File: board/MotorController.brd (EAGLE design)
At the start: 41.6 x 33 mm, 9 parts, among them IC1 7805TV, U1 ATTINY85-20P

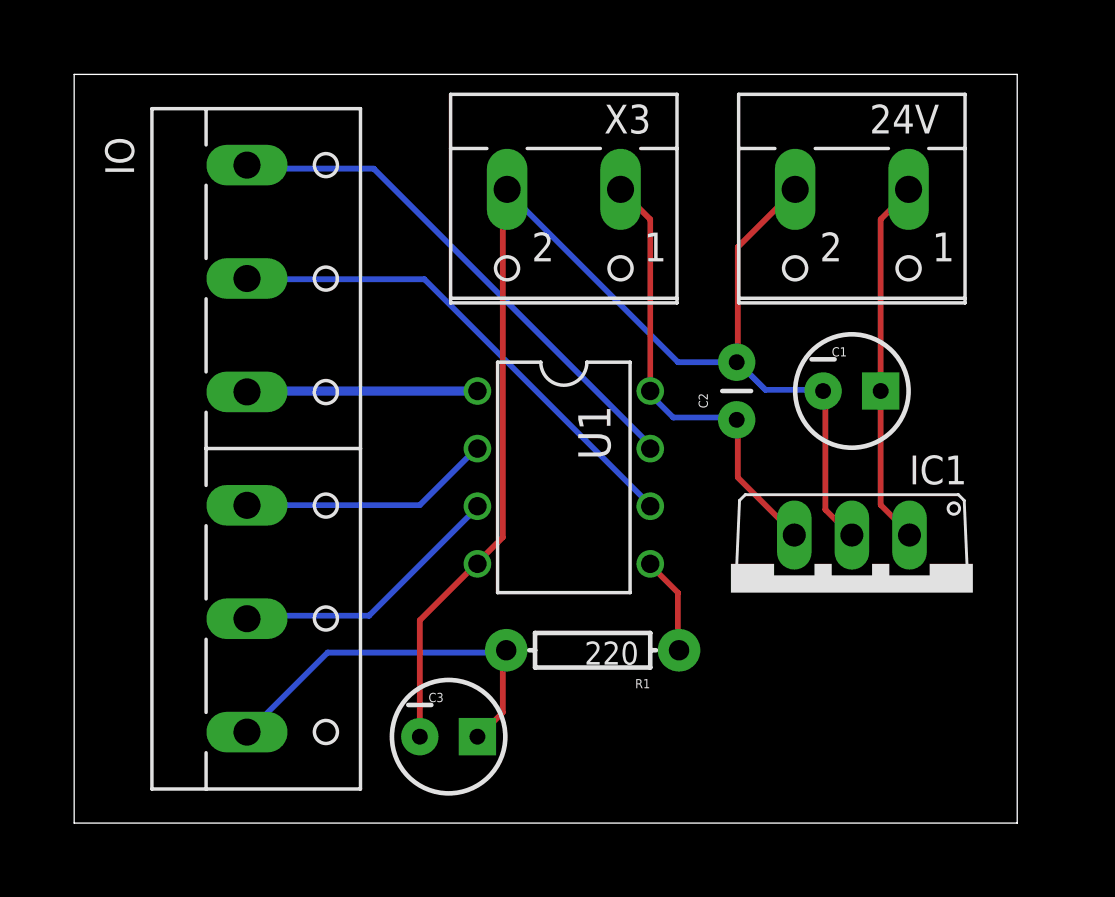
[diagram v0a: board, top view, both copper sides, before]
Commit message: Add a ground pour on the bottom plane and route all power and signal traces on the top
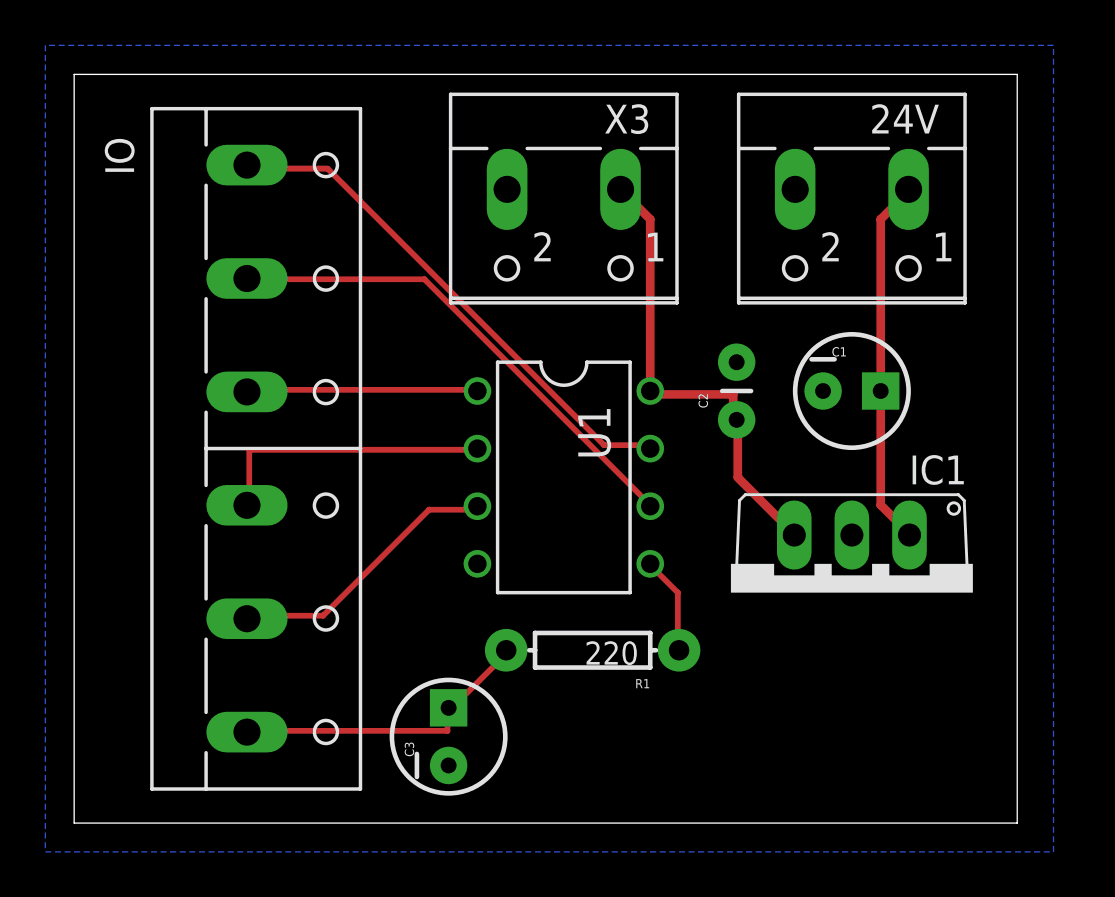
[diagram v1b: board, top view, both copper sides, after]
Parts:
- turned C3 to 90 degrees
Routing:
- net GND: track 59.1 -> 0.00 mm
- net VSPD: track 17.3 -> 13.6 mm
- net N$3: track 11.2 -> 12.6 mm
- net VCC: track 20.0 -> 20.6 mm
- added copper zone on layer 16, net GND

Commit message: Tweaked schematic
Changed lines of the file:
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@@
 <signal name="GND">
 <contactref element="C3" pad="2"/>
-<contactref element="X3" pad="2"/>
 <contactref element="IC1" pad="2"/>
 <contactref element="24V" pad="2"/>
@@
 <vertex x="-1.27" y="34.29"/>
 </polygon>
+<contactref element="X3" pad="2"/>
 </signal>
 <signal name="N$6">
@@
 <contactref element="U1" pad="8"/>
 <contactref element="IC1" pad="3"/>
-<contactref element="X3" pad="1"/>
 <contactref element="C2" pad="1"/>
 <wire x1="29.0576" y1="18.8976" x2="25.4" y2="18.8976" width="0.381" layer="1"/>
@@
 <wire x1="25.4" y1="26.6192" x2="24.1808" y2="27.8384" width="0.381" layer="1"/>
 <wire x1="25.4" y1="19.05" x2="25.4" y2="26.6192" width="0.381" layer="1"/>
-<wire x1="24.1808" y1="27.8384" x2="24.09" y2="27.94" width="0.381" layer="1"/>
+<contactref element="X3" pad="1"/>
+<wire x1="24.1808" y1="27.8384" x2="24.09" y2="27.94" width="0" layer="19" extent="1-1"/>
 </signal>
 <signal name="+24V" class="1">

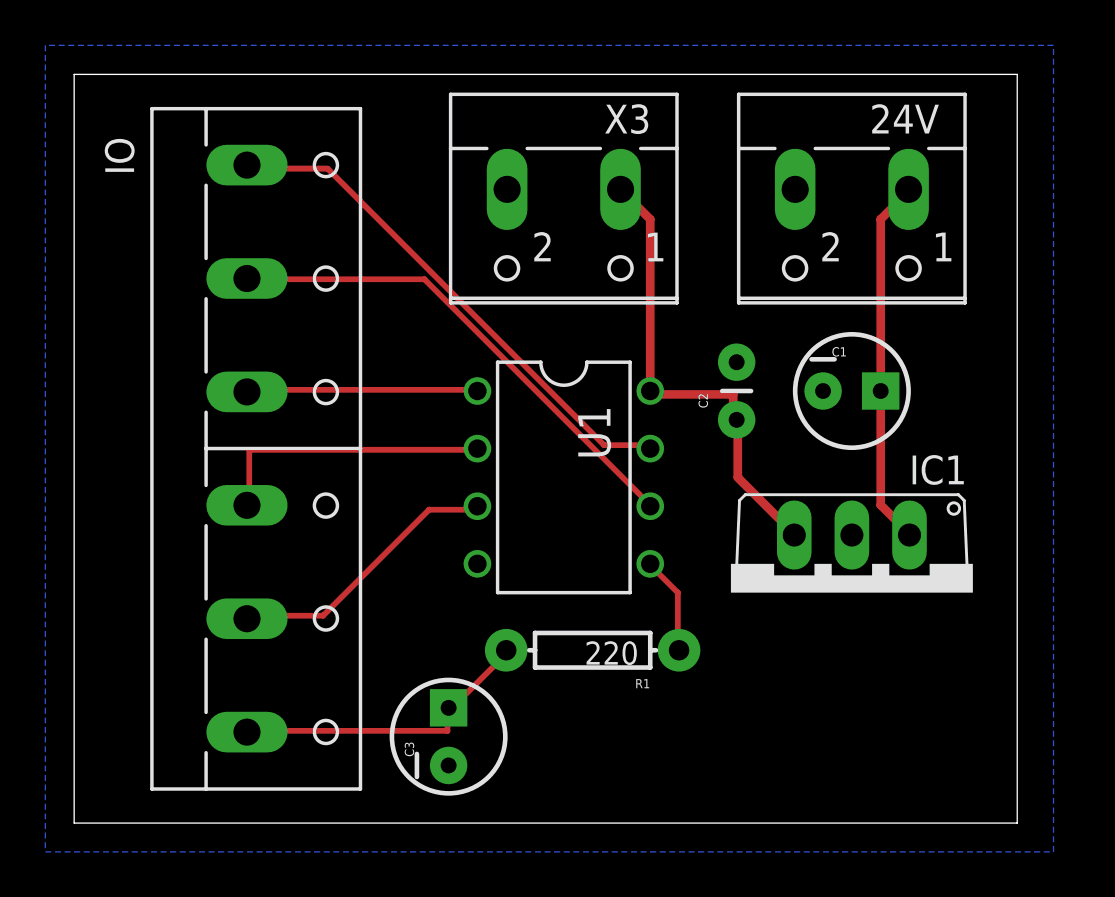
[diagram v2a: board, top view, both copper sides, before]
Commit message: Switch to a top GND pour
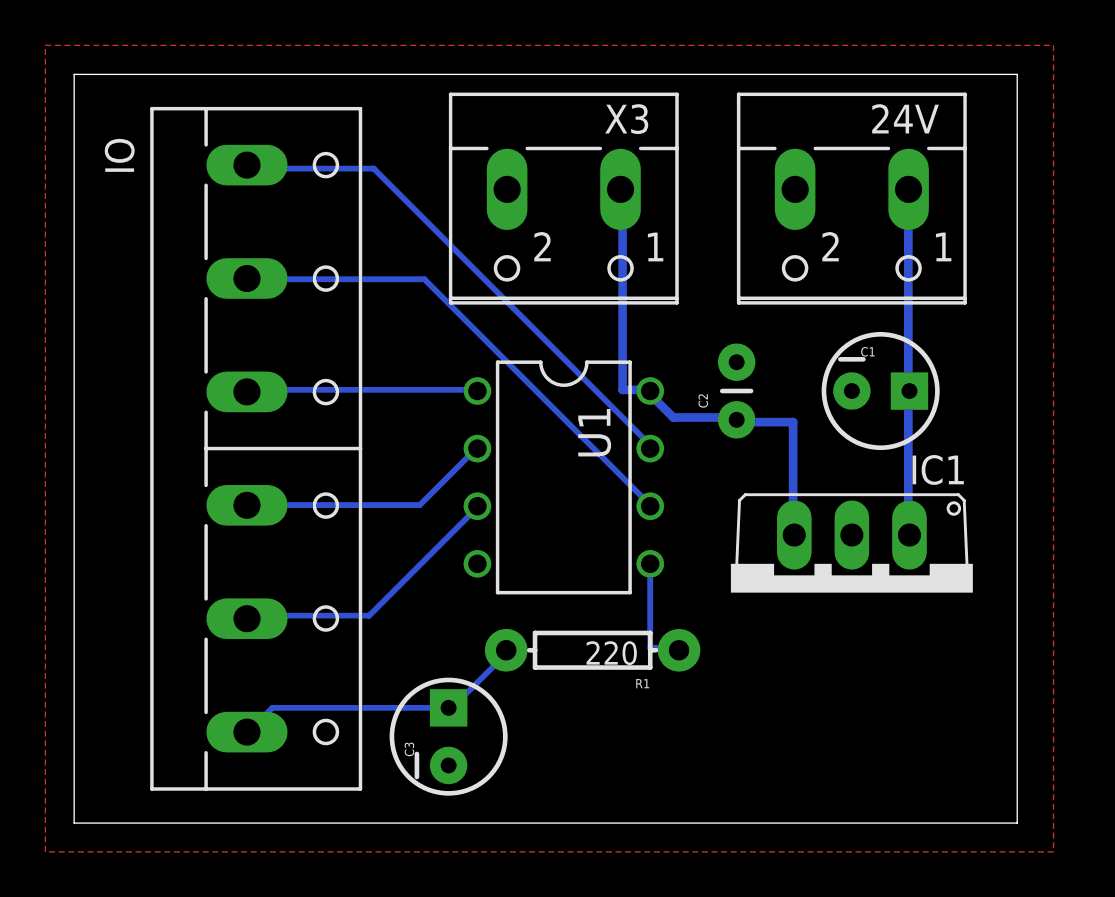
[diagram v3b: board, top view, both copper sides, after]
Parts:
- moved C1 1.27 mm to (35.6, 19.1)
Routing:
- net VCC: track 20.4 -> 22.1 mm
- net N$3: track 12.6 -> 11.2 mm
- net +24V: track 16.3 -> 15.3 mm
- net N$6: track 4.33 -> 5.04 mm
- net VSPD: track 13.6 -> 13.0 mm
- added copper zone on layer 1, net GND
- removed copper zone on layer 16, net GND

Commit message: Switch to a horizontal regulator and change board layout to fit
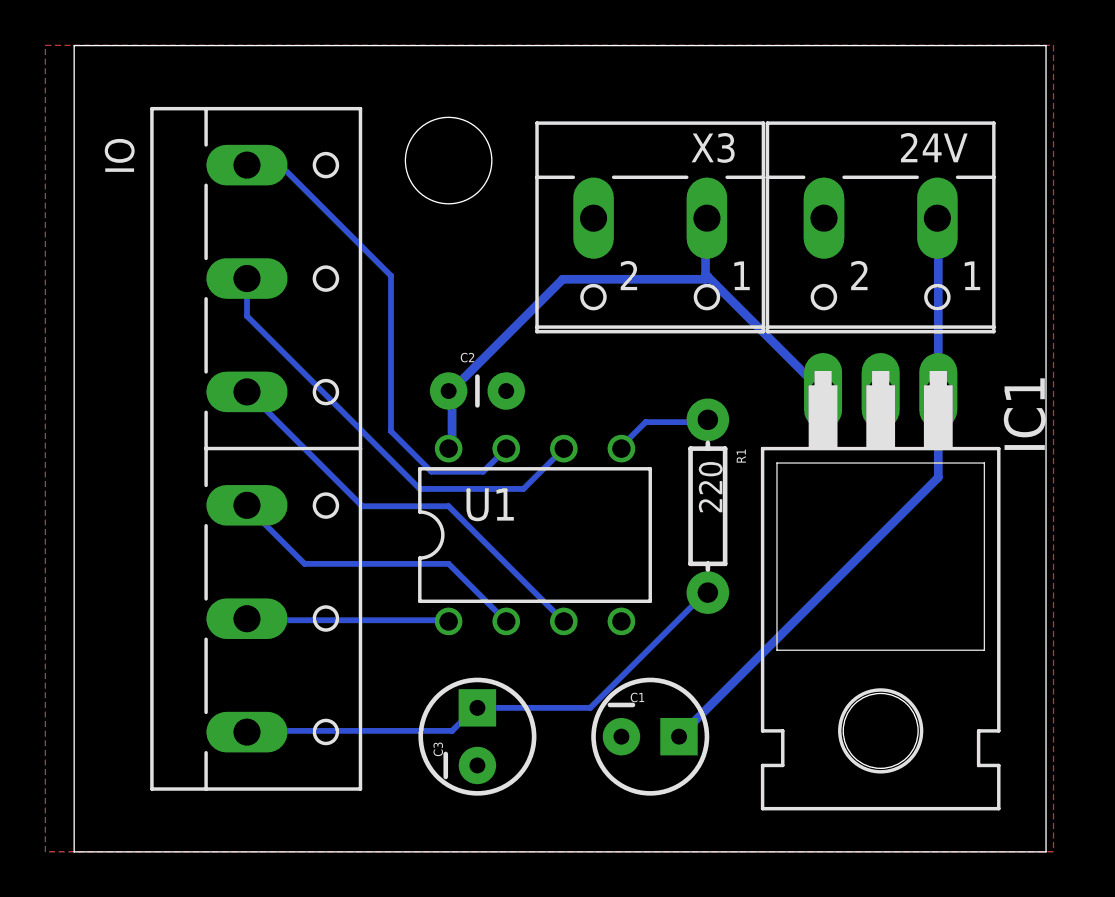
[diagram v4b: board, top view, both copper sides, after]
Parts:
- IC1: value 7805TV -> 7805T; device linear:TO220V -> linear:TO220H
- moved C1 18.3 mm to (25.4, 3.81)
- moved C2 12.8 mm to (16.5, 19.1), turned to 0 degrees
- moved R1 8.13 mm to (27.9, 14.0), turned to 270 degrees
- moved X3 4.02 mm to (25.4, 25.4)
- moved U1 2.84 mm to (20.3, 12.7), turned to 0 degrees
- moved 24V 1.80 mm to (35.6, 25.4)
- moved IC1 1.80 mm to (35.6, 8.89)
- moved C3 1.27 mm to (17.8, 3.81)
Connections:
- removed net N$4 (its old number): IO.5, U1.3
- removed net N$5 (its old number): IO.3, U1.1
- new net N$1: IO.3, U1.3
- new net N$3: IO.5, U1.1
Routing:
- net N$1: track 0.00 -> 18.2 mm
- net +24V: track 15.3 -> 27.6 mm
- net N$4 (its old number): track 12.2 -> 0.00 mm
- net N$5 (its old number): track 10.2 -> 0.00 mm
- net VSPD: track 13.0 -> 22.9 mm
- net N$3: track 0.00 -> 8.93 mm
- net VCC: track 22.1 -> 26.0 mm
- net N$5: track 22.0 -> 19.5 mm
- net N$2: track 11.2 -> 13.6 mm
- net N$4: track 23.1 -> 21.5 mm
- net N$6: track 5.04 -> 4.38 mm
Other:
- board size 41.6 x 33 mm -> 42.9 x 35.6 mm
